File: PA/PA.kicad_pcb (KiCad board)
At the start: 2 copper layers, 100 x 100 mm, 127 parts, among them J1 Conn_Coaxial, J10 Conn_01x01, J11 Conn_01x01, J12 Conn_01x01, J13 Conn_01x01, J14 Conn_01x01, J15 Conn_01x01, J16 Conn_01x01, J17 Conn_01x01, J18 Conn_01x01, J19 Conn_01x01, J2 Conn_01x02, J20 Conn_01x01, J21 Conn_01x01, J22 Conn_01x01, J23 Conn_01x01, J24 Conn_01x01, J25 Conn_01x01, J26 Conn_01x01, J27 Conn_01x01, J28 Conn_01x01, J29 Conn_01x01, J3 Conn_Coaxial, J30 Conn_01x01, J4 Conn_01x02, J5 Conn_01x02, J6 Conn_01x01, J7 Conn_01x01, J8 Conn_01x01, J9 Conn_01x01, Q1 2N3904, Q2 IRF510N, Q3 IRF510N, Q4 2N3906, Q5 TIP42, T1 Transformer_1P1Sdotted, T2 Transformer_1P1Sdotted, T3 Transformer_1P1Sdotted

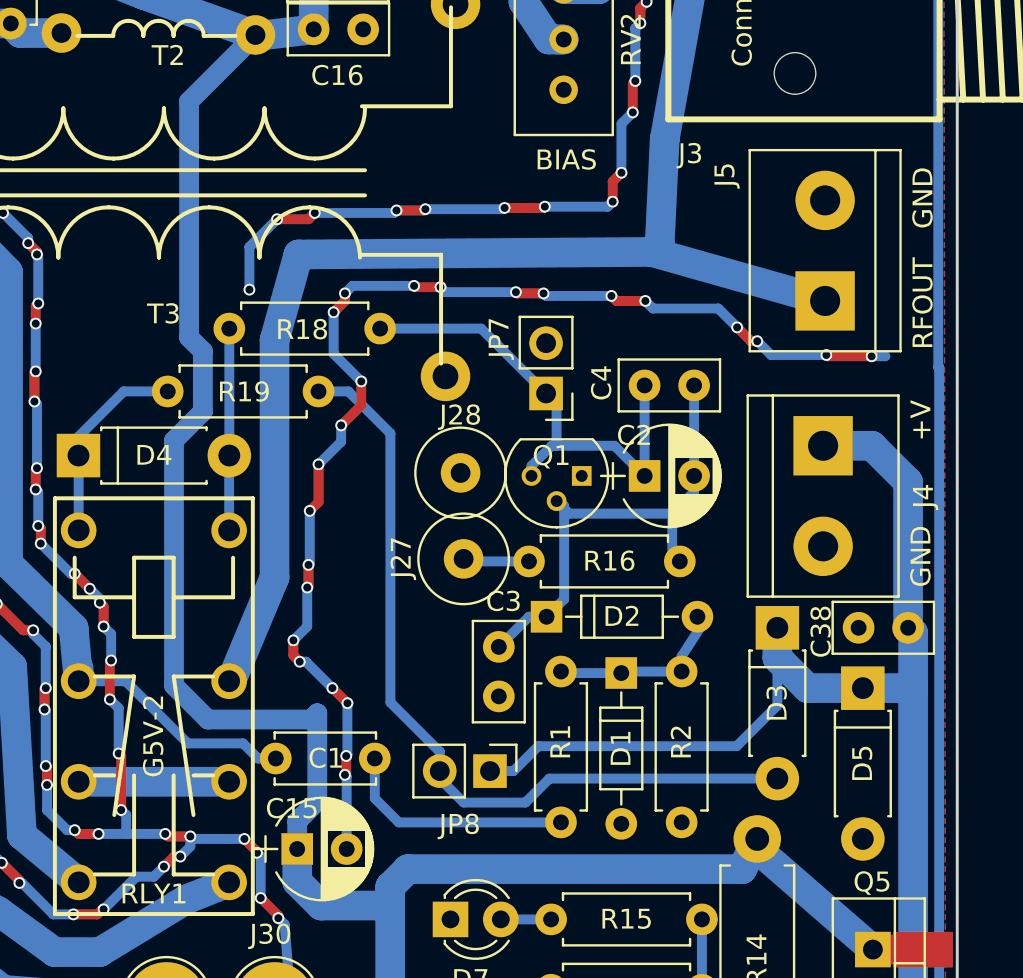
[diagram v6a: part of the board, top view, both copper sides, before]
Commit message: Fixed polarity of rig RXTX relay grounding
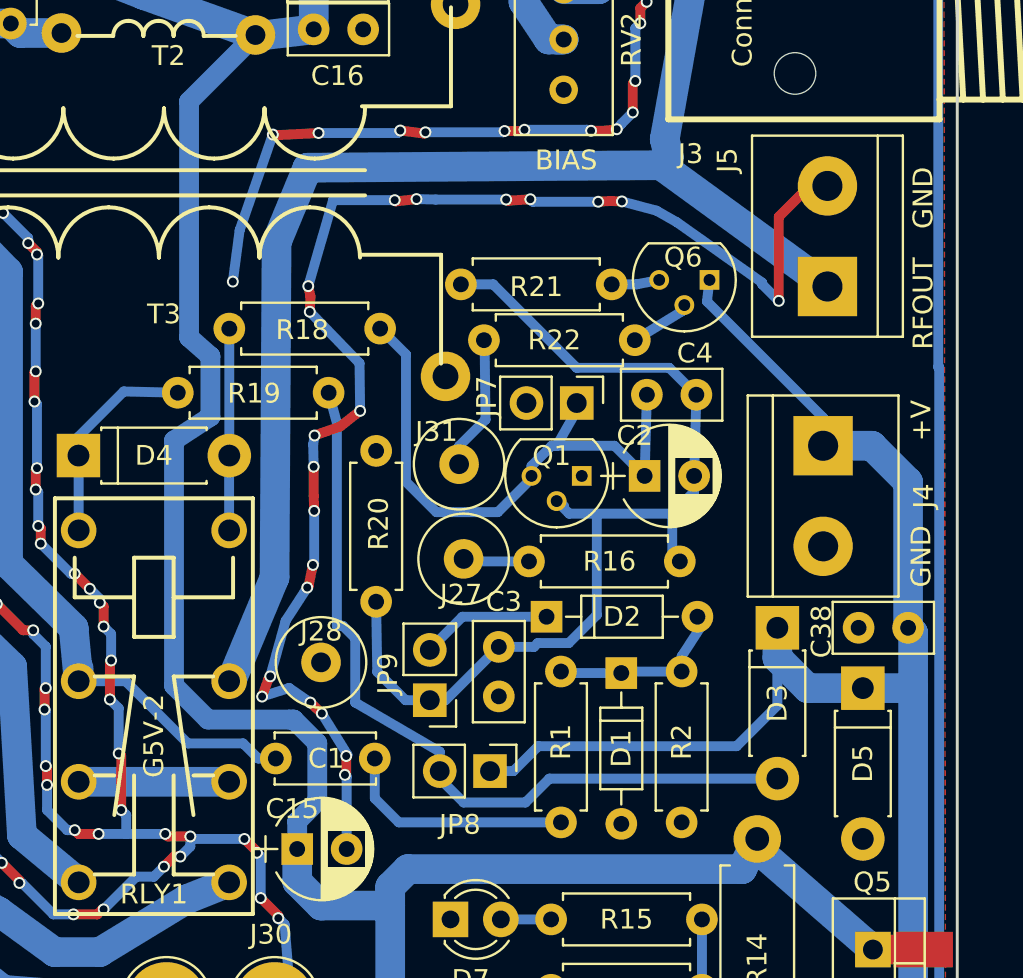
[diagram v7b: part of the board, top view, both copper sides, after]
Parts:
- added J31: Conn_01x01, Connectors:1pin, F.Cu at (114.8, 82.0)
- added JP9: Jumper_NC_Small, Pin_Headers:Pin_Header_Straight_1x02_Pitch2.54mm, F.Cu at (113.4, 93.9)
- added Q6: 2N3906, TO_SOT_Packages_THT:TO-92_Molded_Narrow, F.Cu at (127.5, 72.6)
- added R20: 100k, Resistors_THT:R_Axial_DIN0207_L6.3mm_D2.5mm_P7.62mm_Horizontal, F.Cu at (110.6, 88.9)
- added R21: 470R, Resistors_THT:R_Axial_DIN0207_L6.3mm_D2.5mm_P7.62mm_Horizontal, F.Cu at (122.5, 72.9)
- added R22: 470R, Resistors_THT:R_Axial_DIN0207_L6.3mm_D2.5mm_P7.62mm_Horizontal, F.Cu at (116.1, 75.7)
- moved J28 11.9 mm to (107.9, 92.0)
- moved JP7 1.62 mm to (120.8, 78.9), turned to 270 degrees
- moved J5 0.74 mm to (133.4, 73.0)
- moved R19 0.51 mm to (108.2, 78.3)
- moved C4 0.48 mm to (124.3, 78.4)
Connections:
- D2 pad 1: Net-(C2-Pad2) -> Net-(D2-Pad1)
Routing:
- net Net-(C2-Pad2): track 25.1 -> 52.0 mm
- net +28V: track 90.0 -> 100.8 mm
- net GND: track 547.6 -> 557.7 mm, vias 220 -> 217
- net Net-(J31-Pad1): track 0.00 -> 6.82 mm
- net Net-(D2-Pad1): track 0.00 -> 6.61 mm
- net Net-(C2-Pad1): track 24.4 -> 30.6 mm
- net Net-(Q6-Pad2): track 0.00 -> 3.13 mm
- net Net-(Q6-Pad3): track 0.00 -> 2.42 mm
- net Net-(J3-Pad1): track 63.6 -> 65.1 mm
- net PASUPPLY: track 140.7 -> 140.2 mm
- net Net-(D4-Pad1): track 10.4 -> 10.9 mm
